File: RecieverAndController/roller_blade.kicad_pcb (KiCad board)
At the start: 2 copper layers, 38.1 x 38.1 mm, 48 parts, among them J1 Conn_01x03, J2 Conn_02x03_Counter_Clockwise, J3 Conn_01x03, J4 Conn_01x03, SW1 SW_DIP_x01, U1 ATMEGA328-AU, U2 MAX7036, U3 MLX90365, U4 AP2204_3V3, Y1 16MHz, Y2 13.56MHz

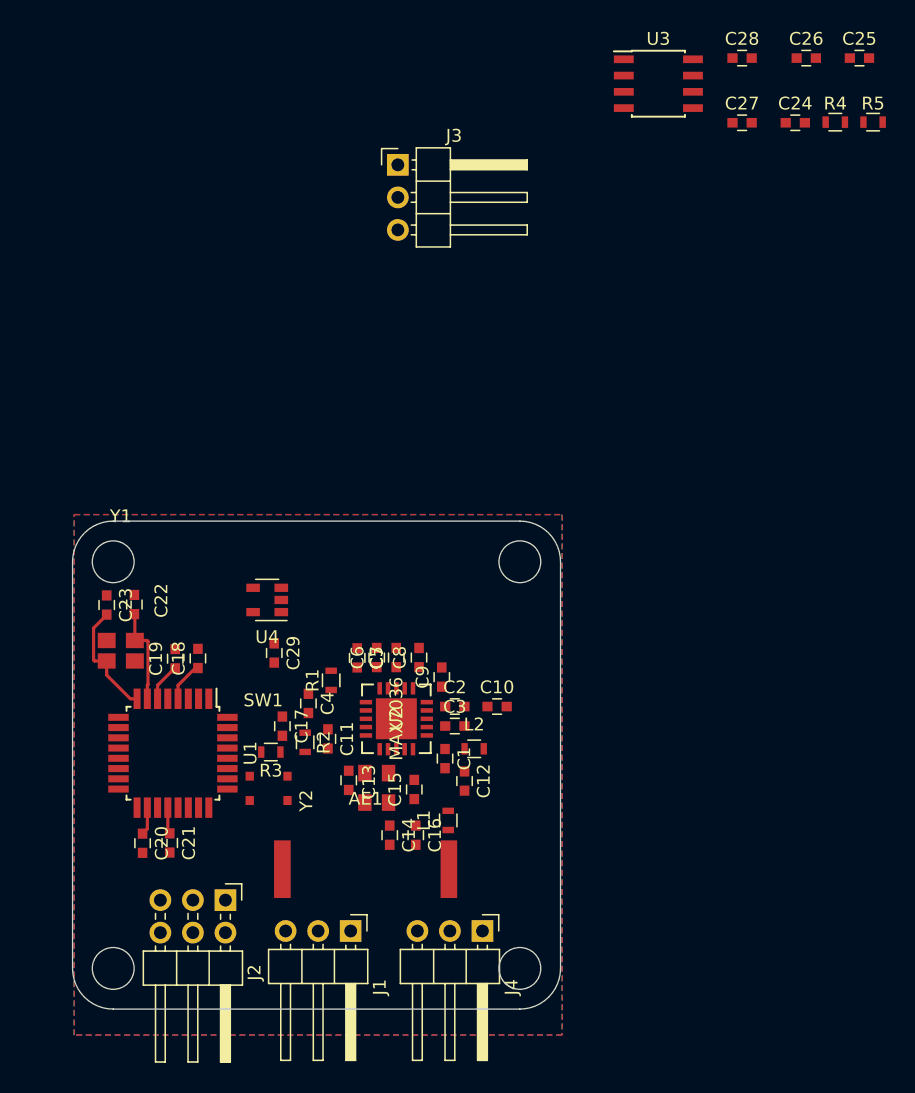
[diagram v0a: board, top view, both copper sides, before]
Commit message: adding and fixing reciever
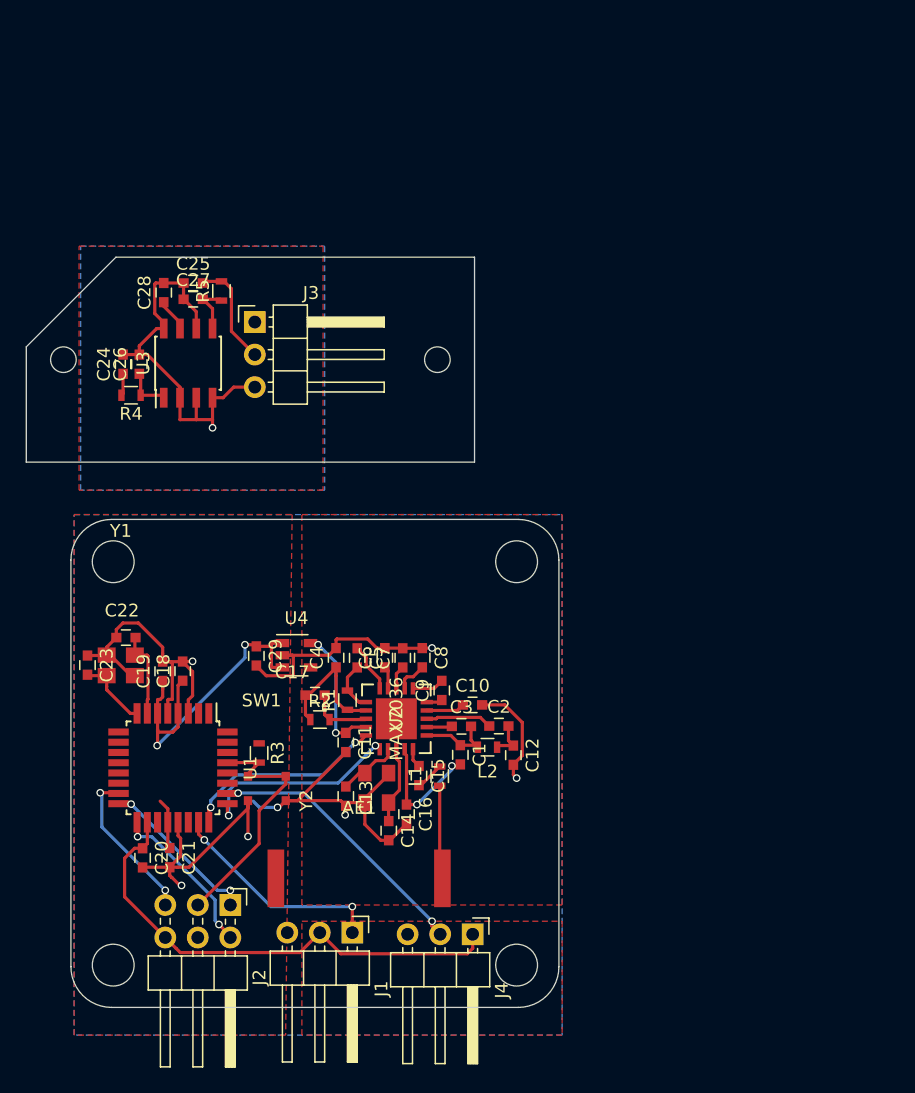
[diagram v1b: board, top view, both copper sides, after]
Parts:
- C1: value 4.7pF -> 2.7pF
- L1: value 100nH -> 47nH
- L2: value 27nH -> 15nH
- moved R4 59.0 mm to (98.4, 98.6), turned to 180 degrees
- moved C26 57.3 mm to (99.1, 96.2), turned to 90 degrees
- moved C24 55.8 mm to (97.8, 96.2), turned to 90 degrees
- moved C25 54.9 mm to (103.3, 89.9)
- moved R5 52.6 mm to (105.5, 90.5), turned to 90 degrees
- moved C28 48.7 mm to (101.0, 90.6), turned to 90 degrees
- moved C27 45.0 mm to (103.3, 91.1)
- moved U3 42.7 mm to (102.9, 96.1), turned to 90 degrees
- moved J3 16.6 mm to (108.1, 92.9)
- moved C23 4.93 mm to (95.0, 119.7)
- moved U4 4.89 mm to (111.3, 118.9), turned to 0 degrees
- moved C12 4.31 mm to (128.3, 126.7)
- moved C4 4.17 mm to (114.4, 119.1), turned to 90 degrees
- moved C2 3.76 mm to (127.1, 124.5)
- moved L1 3.52 mm to (122.5, 128.4)
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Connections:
- C16 pad 1: (no net) -> +3V3
- U1 pad 1: /MCU/PD0 -> (no net)
- U1 pad 10: /MCU/PD0 -> (no net)
- U1 pad 11: /MCU/PD0 -> (no net)
- U1 pad 2: /MCU/PD0 -> (no net)
- U1 pad 30: /MCU/PD0 -> (no net)
- U1 pad 31: /MCU/PD0 -> (no net)
- U1 pad 32: /MCU/PD0 -> (no net)
- U1 pad 9: /MCU/PD0 -> (no net)
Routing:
- net GND: track 0.00 -> 96.1 mm, vias 0 -> 7
- net +5V: track 10.4 -> 70.8 mm, vias 0 -> 2
- net /encoder/GND_L: track 0.00 -> 32.2 mm, vias 0 -> 1
- net +3V3: track 0.00 -> 26.2 mm, vias 0 -> 4
- net /ENC_OUT: track 0.00 -> 21.4 mm, vias 0 -> 2
- net /MCU/RESET: track 0.00 -> 19.8 mm
- net /ESC_SIG: track 0.00 -> 17.3 mm, vias 0 -> 2
- net /REC_EN: track 0.00 -> 16.3 mm, vias 0 -> 2
- net /REC_OUT: track 0.00 -> 16.0 mm, vias 0 -> 2
- net /MCU/MISO: track 0.00 -> 12.7 mm, vias 0 -> 2
- net /MCU/SCK: track 0.00 -> 12.7 mm, vias 0 -> 2
- net /MCU/MOSI: track 0.00 -> 12.3 mm, vias 0 -> 2
- net Net-(C17-Pad1): track 0.00 -> 10.8 mm
- net /encoder/ENC_OUT_L: track 0.00 -> 8.42 mm
- net Net-(AE1-Pad1): track 0.00 -> 7.32 mm
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- added copper zone on F.Cu, net +3V3
- added copper zone on F.Cu, net /encoder/5V_L
- added copper zone on B.Cu, net /encoder/GND_L
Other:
- board size 38.1 x 38.1 mm -> 41.6 x 58.6 mm

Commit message: adding gerber files
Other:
- board text added: "5V"
- board text added: "5V_L"
- board text added: "ENC_ OUT_ L"
- board text added: "ENC_OUT"
- board text added: "ESC_SIG"
- board text added: "GND"
- board text added: "MISO"
- board text added: "MOSI"
- board text added: "RESET"
- board text added: "SCK"
